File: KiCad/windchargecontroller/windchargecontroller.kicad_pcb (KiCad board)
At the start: 2 copper layers, 151.9 x 68.6 mm, 49 parts, among them J1 1935789, J2 1935789, J3 1935789, J4 1935789, J5 ESQ-120-XX-X-D-XX, J6 1935789, Q1 Si7336ADP, Q10 2N5210, Q11 2N5087, Q12 2N5210, Q13 2N5087, Q14 Si7336ADP, Q15 Si7336ADP, Q2 Si7336ADP, Q3 Si7336ADP, Q4 Si7336ADP, Q5 Si7336ADP, Q6 Si7336ADP, Q7 2N5210, Q8 2N5087, Q9 Si7336ADP

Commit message: cleaning up
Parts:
- moved G*** 15.4 mm to (128.8, 77.2)
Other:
- board text removed: "Don't give up, skeleton!"

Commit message: started work on pcb v2.0
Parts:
- moved G*** 47.5 mm to (85.5, 57.5), turned to 90 degrees
- moved Q9 44.1 mm to (183.2, 71.8), turned to 90 degrees
- moved FL1 41.5 mm to (180.8, 54.5), turned to -90 degrees
- moved C13 15.8 mm to (178.2, 46.0), turned to 90 degrees
- moved C15 7.13 mm to (164.0, 45.9), turned to 90 degrees
- moved D1 6.50 mm to (158.5, 55.0), turned to -90 degrees
- moved C14 4.48 mm to (149.8, 45.9)
- moved R7 3.69 mm to (188.2, 39.6)
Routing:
- net GND: track 110.9 -> 63.8 mm
- net /D4_con: track 38.1 -> 0.01 mm
- net /Q6_drive: track 42.8 -> 19.0 mm
- net Power2Out: track 135.0 -> 115.3 mm
- net /Loadswitch: track 19.0 -> 0.00 mm
- net /FL1_con: track 17.1 -> 0.30 mm
- net Shunt7: track 121.3 -> 108.7 mm
- net Shunt2: track 153.5 -> 143.0 mm, vias 1 -> 2
- net /Q11_con: track 9.00 -> 0.07 mm
- net Shunt4: track 91.0 -> 83.6 mm
- net /R9_con: track 19.8 -> 15.0 mm
- net Shunt3: track 87.4 -> 85.4 mm
- net PhaseA+: track 15.1 -> 13.5 mm
- net PhaseB+: track 33.9 -> 35.3 mm
- added copper zone on F.Cu, net /D4_con
- added copper zone on F.Cu, net /Loadswitch
- added copper zone on F.Cu, net /Q11_con
- added copper zone on F.Cu, net /R9_con
- added copper zone on F.Cu, net Power2Out
- added copper zone on F.Cu, net Shunt2
- added copper zone on F.Cu, net Shunt4
- added copper zone on F.Cu, net Shunt7
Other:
- board text added: "WCC V.2.0 K.Q"
- board text removed: "WCC V.1.2 K.Q"

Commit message: started work on Measure Board V1
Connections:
- J5 pad 34: Power1Out -> unconnected-(J5-Pad34)
- J5 pad 40: GND -> Power1Out
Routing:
- net Power1Out: track 81.0 -> 71.5 mm
- net GND: track 63.8 -> 54.7 mm
- net PowerSW1: track 72.9 -> 77.1 mm
- net Shunt5: track 55.1 -> 51.8 mm
- net Shunt3: track 85.4 -> 83.2 mm
- net Shunt4: track 83.6 -> 81.4 mm
- net PWM_sig: track 51.0 -> 50.1 mm
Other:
- board text added: "(VSupp)"
- board text added: "PGND"

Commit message: WCC 2.0
ready for it to be roasted again
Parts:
- added G***: LOGO, LOGO, F.Cu at (167.6, 97.5)
- added G***: LOGO, LOGO, F.Cu at (81.1, 80.9)
- moved C5 28.2 mm to (144.4, 65.5)
- moved C7 23.2 mm to (146.5, 69.8), turned to 90 degrees
- moved C4 21.6 mm to (160.8, 67.6), turned to 90 degrees
- moved C8 20.3 mm to (150.6, 69.8), turned to 90 degrees
- moved C6 19.9 mm to (144.4, 61.9)
- moved C3 18.6 mm to (155.7, 67.6), turned to 90 degrees
- moved C10 13.5 mm to (160.7, 62.6), turned to 90 degrees
- moved C9 9.48 mm to (155.7, 62.6), turned to 90 degrees
- moved R6 8.99 mm to (150.4, 61.1), turned to -90 degrees
- moved D1 4.90 mm to (154.9, 51.7), turned to 0 degrees
- moved C14 4.18 mm to (145.6, 45.8)
- moved Q9 0.56 mm to (183.3, 72.3)
- moved D2 0.39 mm to (195.6, 54.2)
- moved C15 0.19 mm to (164.2, 45.9)
- moved C13 0.09 mm to (178.2, 45.9)
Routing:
- net /R9_con: track 15.0 -> 0.00 mm
- net Shunt2: track 143.0 -> 151.4 mm
- net Power1Out: track 71.5 -> 79.8 mm
- net /Q6_drive: track 19.0 -> 18.4 mm
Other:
- board text added: "D4_con"
- board text added: "FL1_con"
- board text added: "PhaseA+"
- board text added: "PhaseB+"
- board text added: "PhaseC+"
- board text added: "Power1Out"

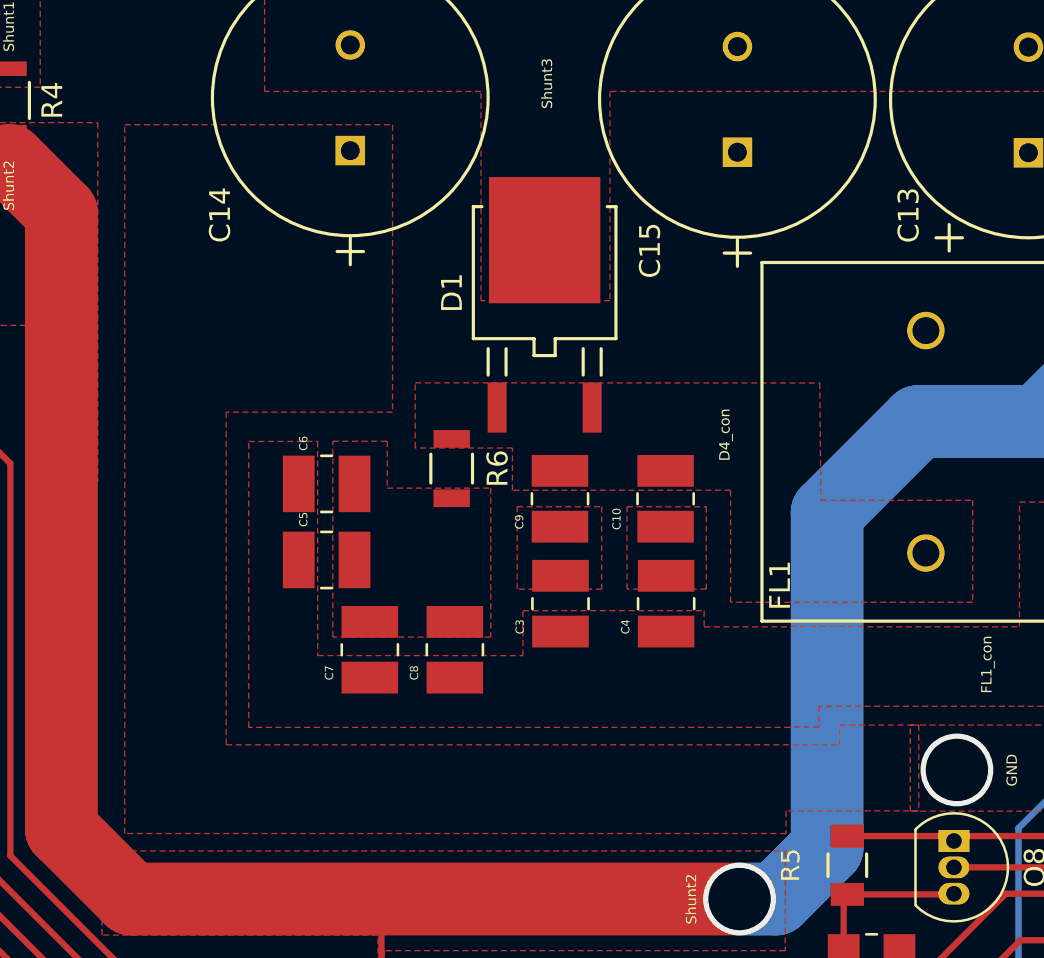
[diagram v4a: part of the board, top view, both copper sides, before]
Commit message: started V2 WMB
fixed PSU issue
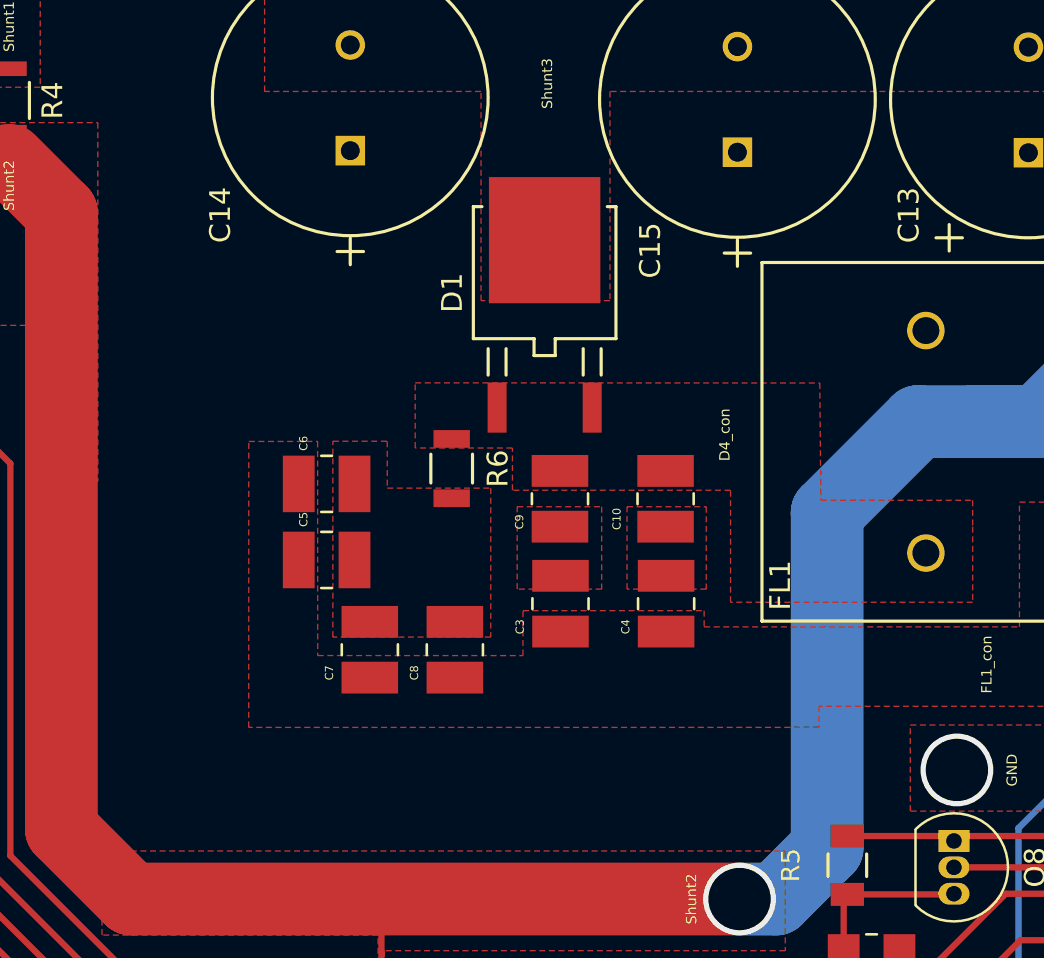
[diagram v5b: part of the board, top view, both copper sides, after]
